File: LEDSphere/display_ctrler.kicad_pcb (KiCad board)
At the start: 4 copper layers, 168 x 131.1 mm, 38 parts, among them J101 CONN_01x02, J301 USB_C_Receptacle_USB2.0, J302 Micro_SD_Card, U1 SN74AHC1G14DBVR, U101 W25Q128JVP, U301 USBLC6-2SC6, U303 RP2040, U305 ESP01s, Y301 12MHz

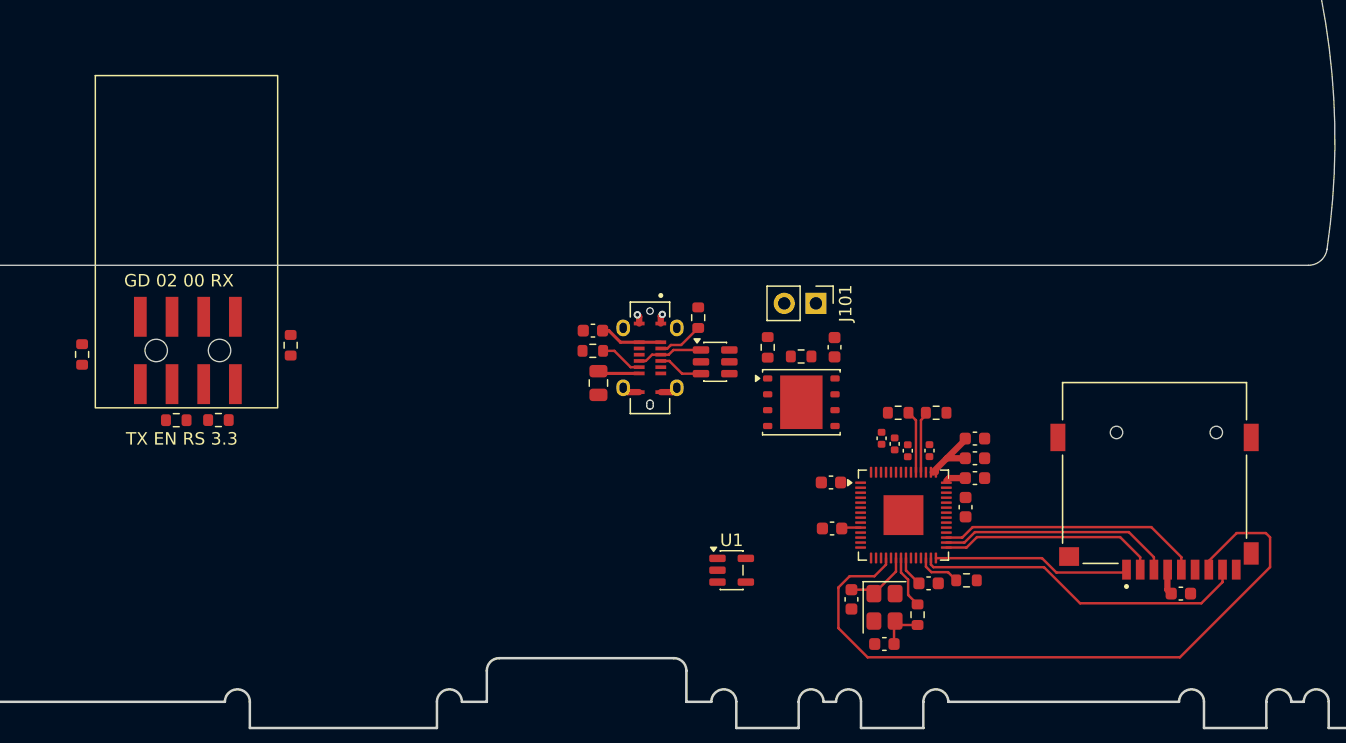
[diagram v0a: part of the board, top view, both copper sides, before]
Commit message: finish display controller layout
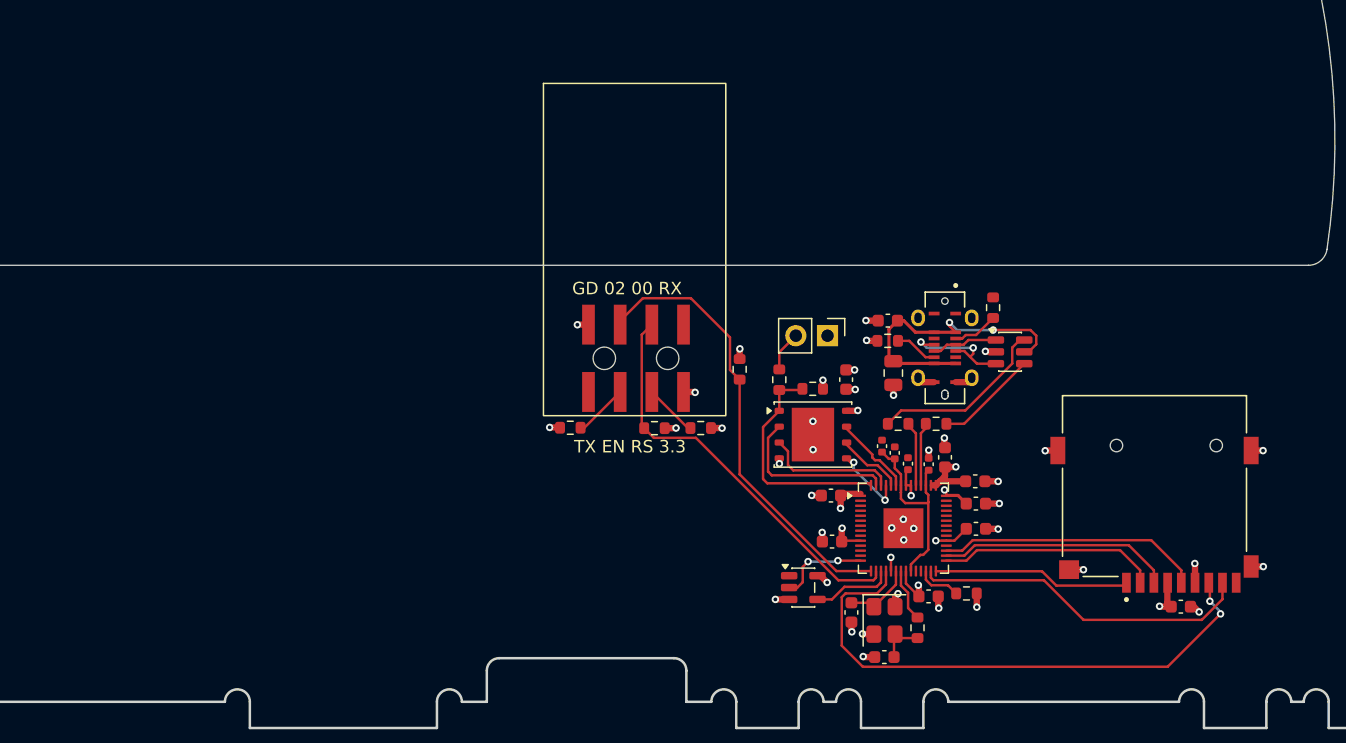
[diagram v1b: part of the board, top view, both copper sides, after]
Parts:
- moved R309 52.7 mm to (160.1, 135.5), turned to 90 degrees
- moved R312 38.7 mm to (157.0, 140.2)
- moved U305 35.9 mm to (151.8, 134.6)
- moved R313 31.6 mm to (146.5, 140.2), turned to 180 degrees
- moved R311 29.9 mm to (153.3, 140.2), turned to 0 degrees
- moved C301 23.7 mm to (172.0, 131.6)
- moved C303 23.7 mm to (172.4, 135.8)
- moved J301 23.7 mm to (176.6, 133.8)
- moved R302 23.7 mm to (180.4, 130.5)
- moved R303 23.7 mm to (172.0, 133.2)
- moved U301 23.7 mm to (181.8, 134.1)
- moved U1 5.91 mm to (165.2, 153.0)
- moved C311 2.83 mm to (176.6, 142.5), turned to -90 degrees
- moved R304 2.76 mm to (166.0, 137.0)
- moved C302 2.76 mm to (168.7, 136.3)
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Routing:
- net I2C0_SDA: track 0.00 -> 36.2 mm
- net I2C0_SCL: track 0.00 -> 33.0 mm
- net GND: track 4.40 -> 33.8 mm, vias 2 -> 33
- net +3.3V: track 13.2 -> 33.8 mm, vias 0 -> 18
- net /QSPI_SS: track 0.00 -> 18.4 mm
- net +1V1: track 0.00 -> 16.0 mm
- net /VBUS4: track 8.39 -> 24.1 mm, vias 0 -> 2
- net /UD_2040+: track 0.00 -> 14.5 mm
- net /QSPI_SD1: track 0.00 -> 13.4 mm
- net SD_DAT0: track 56.0 -> 44.6 mm, vias 0 -> 2
- net /QSPI_SD2: track 0.00 -> 10.6 mm
- net /UD_2040-: track 0.00 -> 8.24 mm
- net Hall: track 0.00 -> 7.34 mm, vias 0 -> 2
- net _Hall_: track 0.00 -> 6.56 mm
- net /QSPI_SD3: track 0.00 -> 6.55 mm
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
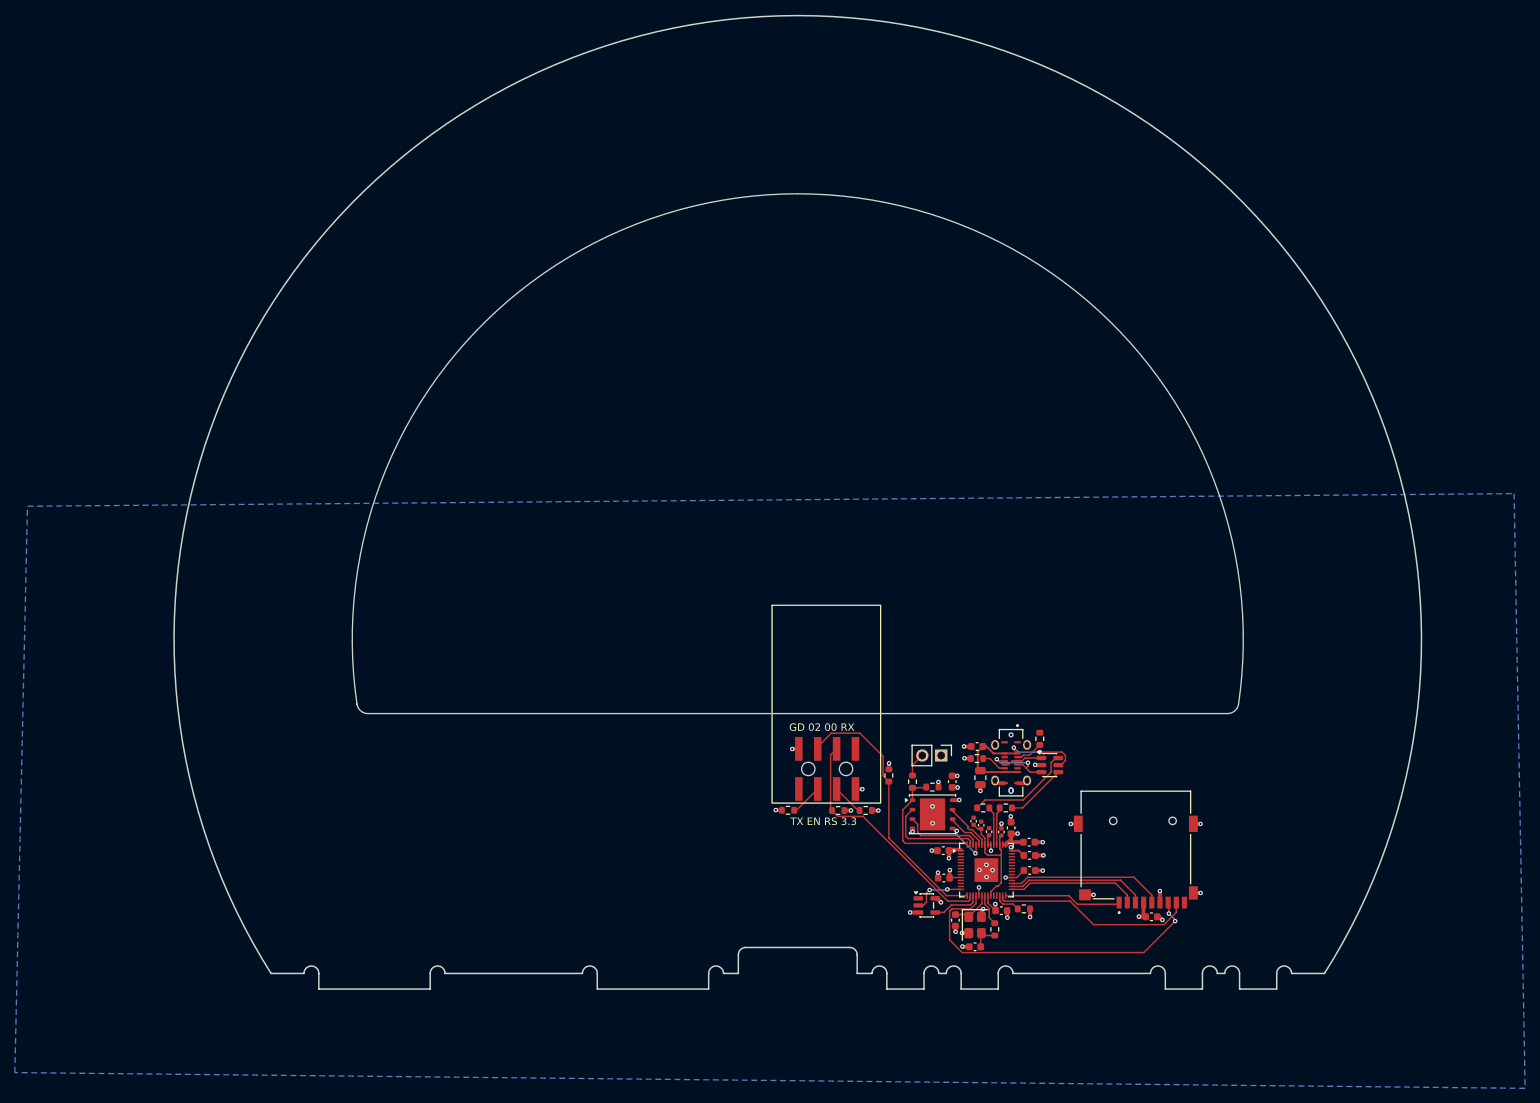
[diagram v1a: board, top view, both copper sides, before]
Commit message: display controller add led terminal
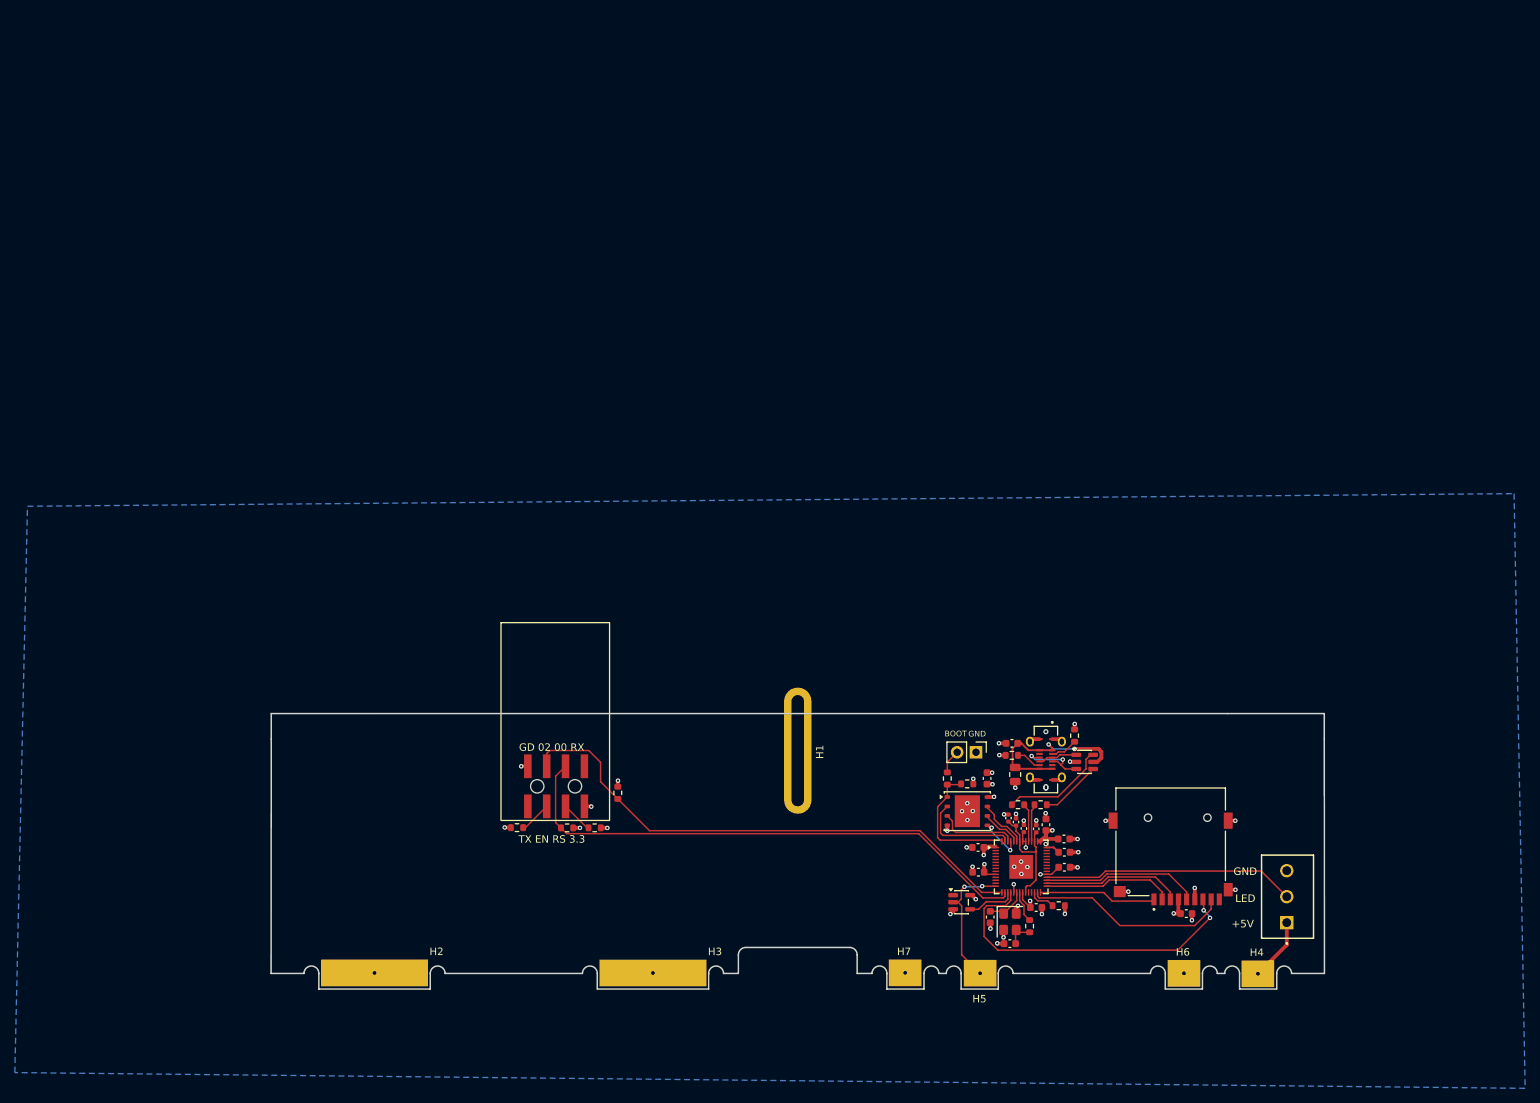
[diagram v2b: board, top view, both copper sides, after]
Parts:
- added H1: middle_slot, Footprints:middle_slot, F.Cu at (147.8, 132.1)
- added H2: edge_contact, Footprints:edge_contact, F.Cu at (90.8, 162.1)
- added H3: edge_contact, Footprints:edge_contact, F.Cu at (128.3, 162.1)
- added H4: small_edge, Footprints:edge_contact_small, F.Cu at (209.8, 162.2)
- added H5: small_edge, Footprints:edge_contact_small, F.Cu at (172.4, 162.1)
- added H6: small_edge, Footprints:edge_contact_small, F.Cu at (199.9, 162.1)
- added H7: small_edge, Footprints:edge_contact_small, F.Cu at (162.3, 162.1)
- added J103: Screw_Terminal_01x03, Footprints:GCT_TAD05-03-1-L-G_REVA, F.Cu at (213.7, 151.8)
- J301: footprint project_lib:CUI_UJ20-C-V-C-1-SMT-TR -> Footprints:CUI_UJ20-C-V-C-1-SMT-TR
- J302: footprint project_lib:CUI_MSD-4-A -> Footprints:CUI_MSD-4-A
- U305: footprint project_lib:ESP01s_SMD -> Footprints:ESP01s_SMD
- moved R309 36.6 mm to (123.6, 137.8)
- moved R311 36.6 mm to (116.8, 142.5)
- moved R312 36.6 mm to (120.5, 142.5)
- moved R313 36.6 mm to (110.0, 142.5)
- moved U305 36.6 mm to (115.3, 136.9)
- moved C316 4.72 mm to (172.2, 148.5)
- moved C301 4.71 mm to (176.7, 131.1)
- moved C302 4.71 mm to (173.3, 135.9)
- moved C306 4.71 mm to (176.4, 158.1)
- moved C309 4.71 mm to (180.0, 142.7)
- moved R306 4.71 mm to (180.6, 139.4)
- moved U101 4.71 mm to (170.7, 140.3)
- moved C314 4.71 mm to (183.8, 145.8)
- moved C305 4.71 mm to (173.8, 154.5)
- moved C307 4.71 mm to (176.2, 141.2)
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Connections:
- U303 pad 13: LED_DATA -> unconnected-(U303-GPIO10-Pad13)
- U303 pad 32: unconnected-(U303-GPIO21-Pad32) -> LED_DATA
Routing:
- net I2C0_SCL: track 33.0 -> 73.5 mm
- net I2C0_SDA: track 36.2 -> 72.6 mm
- net LED_DATA: track 0.00 -> 34.1 mm
- net Hall: track 7.34 -> 18.1 mm
- net +5V: track 0.00 -> 8.49 mm
- net GND: track 33.8 -> 40.7 mm, vias 33 -> 39
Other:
- board size 168 x 131.1 mm -> 141.9 x 37.1 mm
- board text added: "+5V"
- board text added: "BOOT"
- board text added: "GND"
- board text added: "LED"

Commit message: adjust positions
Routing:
- net SD_DAT0: track 44.8 -> 50.9 mm

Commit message: move edge connections to correct area
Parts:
- moved H4 37.5 mm to (172.4, 162.1)
- moved H5 27.4 mm to (199.8, 162.1)
- moved H6 9.97 mm to (209.8, 162.1)
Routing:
- net +5V: track 8.49 -> 44.2 mm
- net Hall: track 18.1 -> 43.6 mm, vias 2 -> 4
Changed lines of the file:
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@@
 			(unlocked yes)
 			(layer "F.SilkS")
+			(hide yes)
 			(effects
 				(font
@@
 	(footprint "Footprints:edge_contact_small"
 		(layer "F.Cu")
-		(at 209.82 162.18)
+		(at 172.36 162.14)
 		(property "Reference" "H4"
 			(at -0.15 -2.86 0)
 			(unlocked yes)
 			(layer "F.SilkS")
+			(hide yes)
 			(effects
 				(font
@@
 			(unlocked yes)
 			(layer "F.SilkS")
+			(hide yes)
 			(effects
 				(font
@@
 			(unlocked yes)
 			(layer "F.SilkS")
+			(hide yes)
 			(effects
 				(font
@@
 	(footprint "Footprints:edge_contact_small"
 		(layer "F.Cu")
-		(at 172.41 162.11)
+		(at 199.81 162.11)
 		(property "Reference" "H5"
 			(at -0.09 3.46 0)
 			(unlocked yes)
 			(layer "F.SilkS")
+			(hide yes)
 			(effects
 				(font
@@
 	(footprint "Footprints:edge_contact_small"
 		(layer "F.Cu")
-		(at 199.86 162.13)
+		(at 209.83 162.13)
 		(property "Reference" "H6"
 			(at -0.15 -2.86 0)
 			(unlocked yes)
 			(layer "F.SilkS")
+			(hide yes)
 			(effects
 				(font
@@
 	)
 	(segment
-		(start 213.71 155.2975)
-		(end 213.71 158.29)
+		(start 212.3535 156.654)
+		(end 213.71 155.2975)
 		(width 0.508)
 		(layer "F.Cu")
@@
 	)
 	(segment
-		(start 213.71 158.29)
-		(end 209.82 162.18)
+		(start 172.36 162.14)
+		(end 174.946 159.554)
+		(width 0.508)
+		(layer "F.Cu")
+		(net "+5V")
+	)
+	(segment
+		(start 191.469474 156.654)
+		(end 212.3535 156.654)
+		(width 0.508)
+		(layer "F.Cu")
+		(net "+5V")
+	)
+	(segment
+		(start 188.569474 159.554)
+		(end 191.469474 156.654)
+		(width 0.508)
+		(layer "F.Cu")
+		(net "+5V")
+	)
+	(segment
+		(start 174.946 159.554)
+		(end 188.569474 159.554)
 		(width 0.508)
 		(layer "F.Cu")
@@
 	)
 	(segment
+		(start 169.440749 152.54925)
+		(end 168.77825 152.54925)
+		(width 0.2)
+		(layer "F.Cu")
+		(net "Hall")
+	)
+	(segment
 		(start 172.68575 150.38925)
 		(end 172.6865 150.39)
@@
 	)
 	(segment
-		(start 169.92 159.62)
-		(end 169.92 153.028501)
+		(start 169.75 152.858501)
+		(end 169.440749 152.54925)
+		(width 0.2)
+		(layer "F.Cu")
+		(net "Hall")
+	)
+	(segment
+		(start 169.75 156.04)
+		(end 169.75 152.858501)
+		(width 0.2)
+		(layer "F.Cu")
+		(net "Hall")
+	)
+	(segment
+		(start 172.450279 158.740279)
+		(end 169.75 156.04)
+		(width 0.2)
+		(layer "F.Cu")
+		(net "Hall")
+	)
+	(segment
+		(start 198.008 160.308)
+		(end 178.49 160.308)
 		(width 0.2)
 		(layer "F.Cu")
@@
 	)
 	(segment
-		(start 169.92 153.028501)
-		(end 169.440749 152.54925)
+		(start 173.679721 158.740279)
+		(end 172.450279 158.740279)
 		(width 0.2)
 		(layer "F.Cu")
@@
 	)
 	(segment
-		(start 169.440749 152.54925)
-		(end 169.869 152.120999)
+		(start 199.81 162.11)
+		(end 198.008 160.308)
 		(width 0.2)
 		(layer "F.Cu")
@@
 	)
 	(segment
-		(start 172.41 162.11)
-		(end 169.92 159.62)
+		(start 169.440749 152.54925)
+		(end 169.869 152.120999)
 		(width 0.2)
 		(layer "F.Cu")
@@
 		(net "Hall")
 	)
-	(segment
-		(start 169.440749 152.54925)
-		(end 168.77825 152.54925)
-		(width 0.2)
-		(layer "F.Cu")
+	(via
+		(at 173.679721 158.740279)
+		(size 0.6)
+		(drill 0.3)
+		(layers "F.Cu" "B.Cu")
 		(net "Hall")
 	)
@@
 		(net "Hall")
 	)
+	(via
+		(at 178.49 160.308)
+		(size 0.6)
+		(drill 0.3)
+		(layers "F.Cu" "B.Cu")
+		(net "Hall")
+	)
 	(segment
 		(start 172.60575 150.46925)
@@
 	)
 	(segment
+		(start 173.71 158.71)
+		(end 176.892 158.71)
+		(width 0.2)
+		(layer "B.Cu")
+		(net "Hall")
+	)
+	(segment
+		(start 173.679721 158.740279)
+		(end 173.71 158.71)
+		(width 0.2)
+		(layer "B.Cu")
+		(net "Hall")
+	)
+	(segment
 		(start 170.29575 150.46925)
 		(end 172.60575 150.46925)
@@
 	)
 	(segment
+		(start 176.892 158.71)
+		(end 178.49 160.308)
+		(width 0.2)
+		(layer "B.Cu")
+		(net "Hall")
+	)
+	(segment
 		(start 173.21575 152.48925)
 		(end 172.20575 153.49925)
@@
 	)
 	(segment
-		(start 204.435 153.59)
-		(end 199.025 159)
+		(start 202.4215 151.0785)
+		(end 202.4215 152.1625)
 		(width 0.2)
 		(layer "F.Cu")
@@
 	)
 	(segment
-		(start 202.4215 151.0785)
-		(end 202.4215 152.1625)
+		(start 175.82575 153.01925)
+		(end 176.5415 152.3035)
 		(width 0.2)
 		(layer "F.Cu")
@@
 	)
 	(segment
-		(start 172.94 153.376304)
-		(end 173.297054 153.01925)
+		(start 172.94 157.152029)
+		(end 172.94 153.376304)
 		(width 0.2)
 		(layer "F.Cu")
@@
 	)
 	(segment
-		(start 205.44 153.64)
-		(end 205.39 153.59)
+		(start 204.61 150.862498)
+		(end 202.637502 150.862498)
 		(width 0.2)
 		(layer "F.Cu")
@@
 	)
 	(segment
-		(start 204.61 150.862498)
-		(end 202.637502 150.862498)
+		(start 191.24 156.1)
+		(end 188.34 159)
 		(width 0.2)
 		(layer "F.Cu")
@@
 	)
 	(segment
-		(start 172.94 157.152029)
-		(end 172.94 153.376304)
+		(start 173.297054 153.01925)
+		(end 175.82575 153.01925)
+		(width 0.2)
+		(layer "F.Cu")
+		(net "SD_DAT0")
+	)
+	(segment
+		(start 172.94 153.376304)
+		(end 173.297054 153.01925)
 		(width 0.2)
 		(layer "F.Cu")
@@
 	)
 	(segment
-		(start 175.82575 153.01925)
-		(end 176.5415 152.3035)
+		(start 205.44 153.64)
+		(end 205.39 153.59)
 		(width 0.2)
 		(layer "F.Cu")
@@
 	)
 	(segment
-		(start 174.787971 159)
-		(end 172.94 157.152029)
+		(start 188.34 159)
+		(end 174.787971 159)
 		(width 0.2)
 		(layer "F.Cu")
@@
 	)
 	(segment
-		(start 199.025 159)
-		(end 174.787971 159)
+		(start 204.435 153.59)
+		(end 201.925 156.1)
 		(width 0.2)
 		(layer "F.Cu")
@@
 	)
 	(segment
-		(start 173.297054 153.01925)
-		(end 175.82575 153.01925)
+		(start 205.39 153.59)
+		(end 204.435 153.59)
 		(width 0.2)
 		(layer "F.Cu")
@@
 	)
 	(segment
-		(start 205.39 153.59)
-		(end 204.435 153.59)
+		(start 201.925 156.1)
+		(end 191.24 156.1)
+		(width 0.2)
+		(layer "F.Cu")
+		(net "SD_DAT0")
+	)
+	(segment
+		(start 174.787971 159)
+		(end 172.94 157.152029)
 		(width 0.2)
 		(layer "F.Cu")

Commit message: change footprints
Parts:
- removed U101: W25Q128JVP, Package_SON:WSON-8-1EP_6x5mm_P1.27mm_EP3.4x4.3mm
- added U102: W25Q128JVS, Package_SO:SOIC-8_5.3x5.3mm_P1.27mm, F.Cu at (170.1, 140.6)
- C303: value 10µF -> 10uF; footprint Capacitor_SMD:C_0805_2012Metric -> Capacitor_SMD:C_1206_3216Metric
- moved C303 0.63 mm to (176.8, 135.9), turned to 90 degrees
- moved C308 0.07 mm to (177.3, 141.7)
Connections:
- C303 pad 1: /VBUS4 -> GND
- C303 pad 2: GND -> /VBUS4
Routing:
- net GND: track 41.1 -> 38.0 mm, vias 39 -> 35
- net /QSPI_SS: track 18.4 -> 20.8 mm
- net /QSPI_SD0: track 5.97 -> 7.97 mm
- net /QSPI_SD1: track 13.4 -> 15.1 mm
- net +3.3V: track 34.1 -> 34.9 mm
- net /QSPI_SD2: track 10.6 -> 11.3 mm
- net /VBUS4: track 24.5 -> 25.1 mm
- net /QSPI_SCLK: track 5.39 -> 4.87 mm
